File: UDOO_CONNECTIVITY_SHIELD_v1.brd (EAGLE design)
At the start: 121.6 x 53.6 mm, 22 parts, among them U1 XBEE

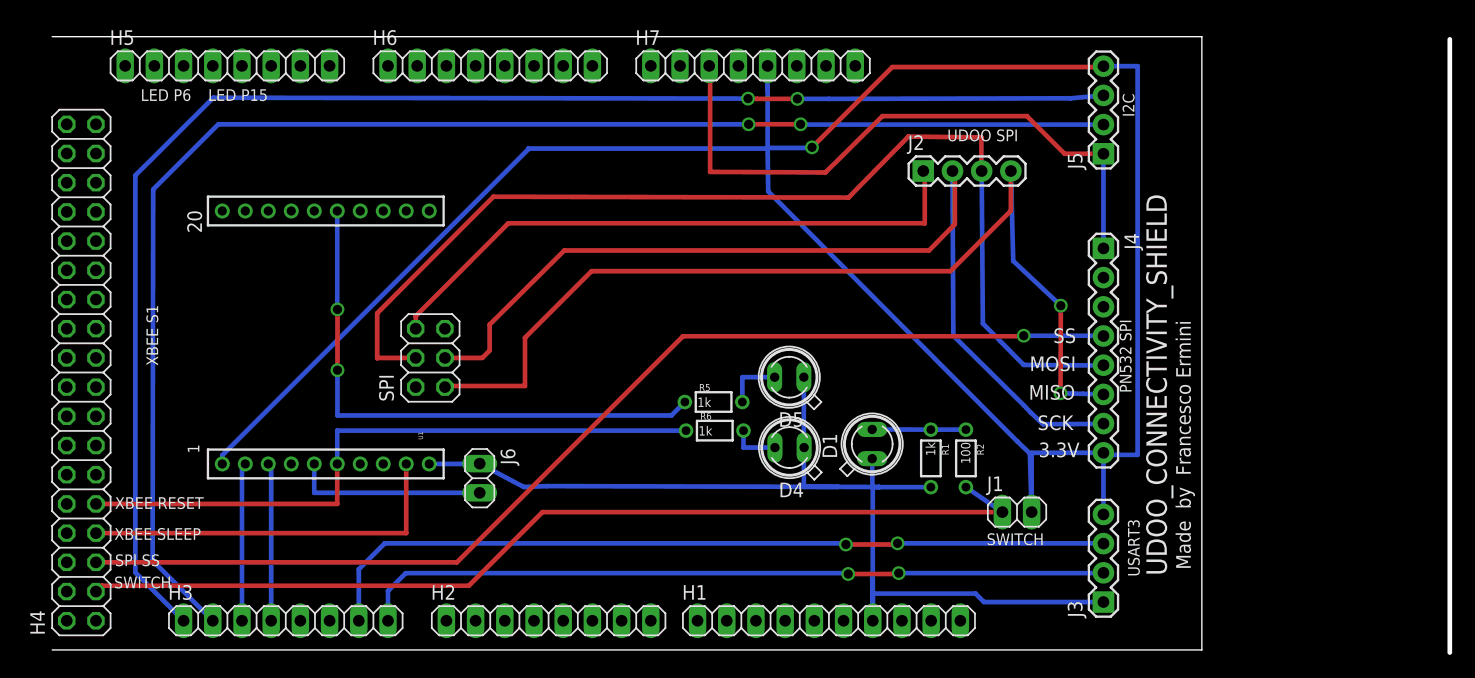
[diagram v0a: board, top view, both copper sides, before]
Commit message: Add link from GPIO_3 (pin 31) to NFC IRQ pin
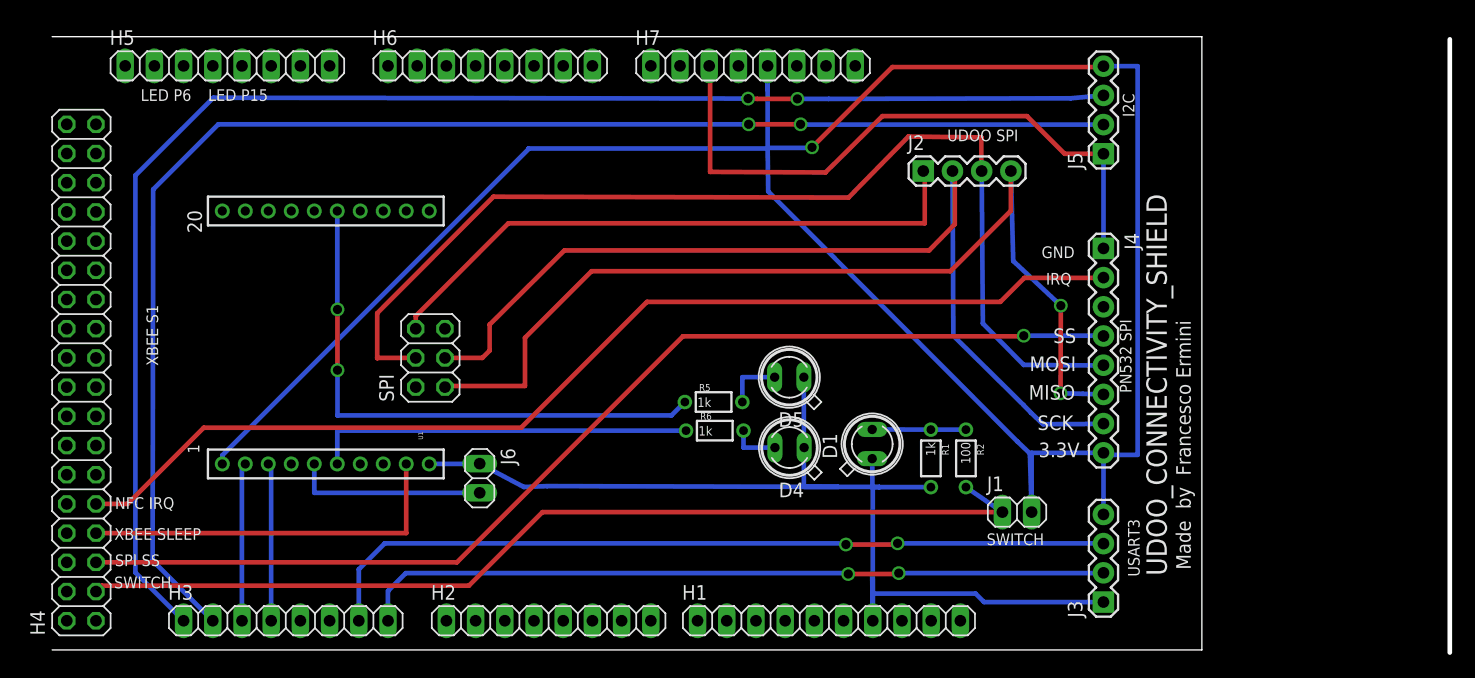
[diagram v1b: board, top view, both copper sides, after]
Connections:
- new net S$18: H4.9, J4.2
- net S$17: no longer H4.9
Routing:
- net S$18: track 0.00 -> 95.8 mm
- net S$17: track 57.7 -> 33.2 mm
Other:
- board text added: "IRQ"
- board text added: "NFC IRQ"
- board text removed: "XBEE RESET"
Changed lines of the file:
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@@
 <text x="5.3848" y="5.3594" size="1.016" layer="25">SWITCH</text>
 <text x="5.4102" y="9.5758" size="1.016" layer="25">XBEE SLEEP</text>
-<text x="5.461" y="12.2682" size="1.016" layer="25">XBEE RESET</text>
+<text x="5.461" y="12.2682" size="1.016" layer="25">NFC IRQ</text>
 <text x="99.0346" y="6.985" size="1.27" layer="25" rot="R90">Made  by  Francesco Ermini</text>
 <text x="77.851" y="44.2468" size="1.016" layer="25">UDOO SPI</text>
@@
 <wire x1="99.9998" y1="0" x2="99.9998" y2="53.34" width="0" layer="20"/>
 <wire x1="99.9998" y1="53.34" x2="0" y2="53.34" width="0" layer="20"/>
+<text x="86.4362" y="31.7754" size="1.016" layer="25">IRQ</text>
+<text x="86.0552" y="34.0868" size="1.016" layer="25">GND</text>
 </plain>
 <attributes>
@@
 <signal name="S$17">
 <contactref element="U1" pad="6"/>
-<contactref element="H4" pad="9"/>
-<wire x1="3.81" y1="12.7" x2="24.798" y2="12.7" width="0.4064" layer="1"/>
-<wire x1="24.798" y1="12.7" x2="24.798" y2="16.178" width="0.4064" layer="1"/>
 <contactref element="R6" pad="1"/>
 <wire x1="24.798" y1="16.178" x2="24.798" y2="19.0754" width="0.4064" layer="16"/>
@@
 <wire x1="91.4146" y1="27.3304" x2="91.44" y2="27.305" width="0.4064" layer="16"/>
 </signal>
+<signal name="S$18">
+<contactref element="J4" pad="2"/>
+<contactref element="H4" pad="9"/>
+<wire x1="3.81" y1="12.7" x2="6.5532" y2="12.7" width="0.4064" layer="1"/>
+<wire x1="6.5532" y1="12.7" x2="13.1826" y2="19.3294" width="0.4064" layer="1"/>
+<wire x1="13.1826" y1="19.3294" x2="40.7924" y2="19.3294" width="0.4064" layer="1"/>
+<wire x1="40.7924" y1="19.3294" x2="51.7398" y2="30.2768" width="0.4064" layer="1"/>
+<wire x1="51.7398" y1="30.2768" x2="82.4738" y2="30.2768" width="0.4064" layer="1"/>
+<wire x1="82.4738" y1="30.2768" x2="84.5566" y2="32.3596" width="0.4064" layer="1"/>
+<wire x1="84.5566" y1="32.3596" x2="91.4146" y2="32.3596" width="0.4064" layer="1"/>
+<wire x1="91.4146" y1="32.3596" x2="91.44" y2="32.385" width="0.4064" layer="1"/>
+</signal>
 </signals>
